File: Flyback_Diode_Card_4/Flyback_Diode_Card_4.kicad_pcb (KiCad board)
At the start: 2 copper layers, 68 parts, among them J1 Screw_Terminal_01x06, J2 Screw_Terminal_01x06, J3 Screw_Terminal_01x02, J4 Screw_Terminal_01x12, J5 Screw_Terminal_01x12, J6 Screw_Terminal_01x04, J7 Screw_Terminal_01x02, J8 Screw_Terminal_01x02

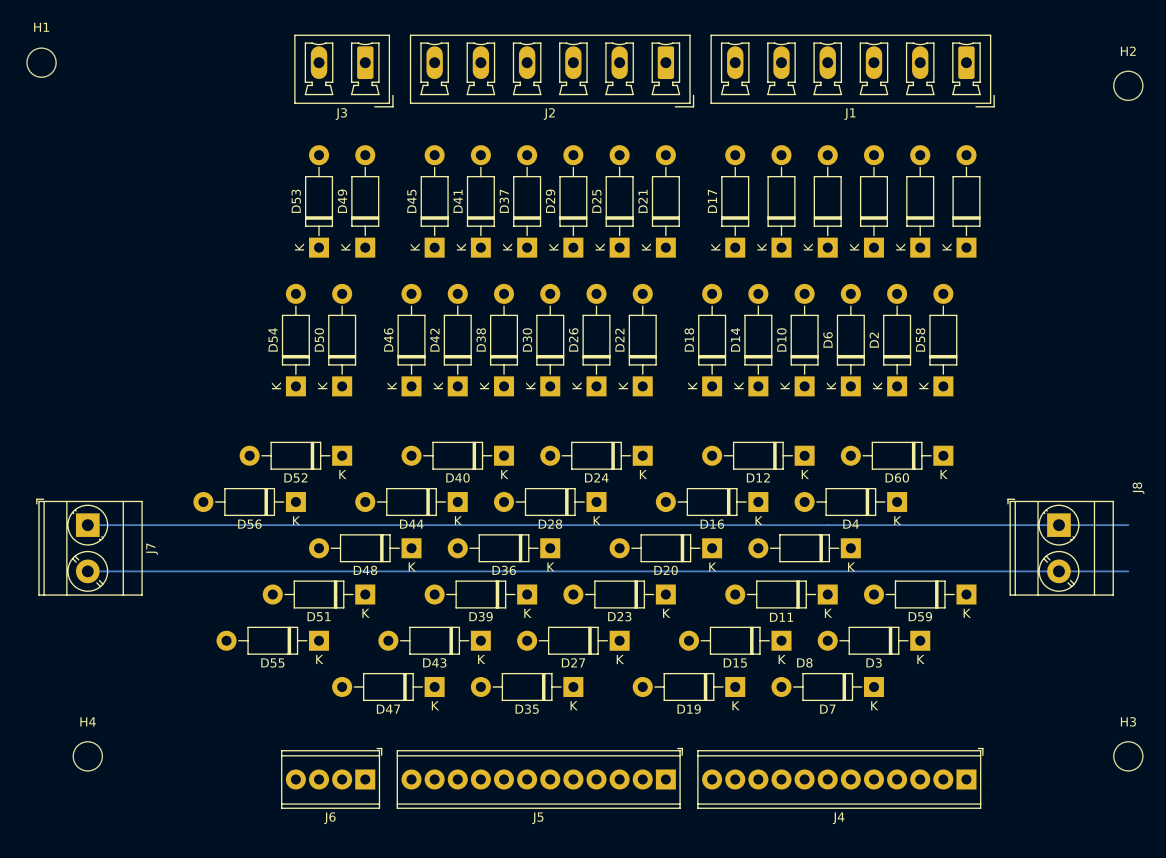
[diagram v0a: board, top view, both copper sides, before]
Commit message: Working on new flyback diode card/
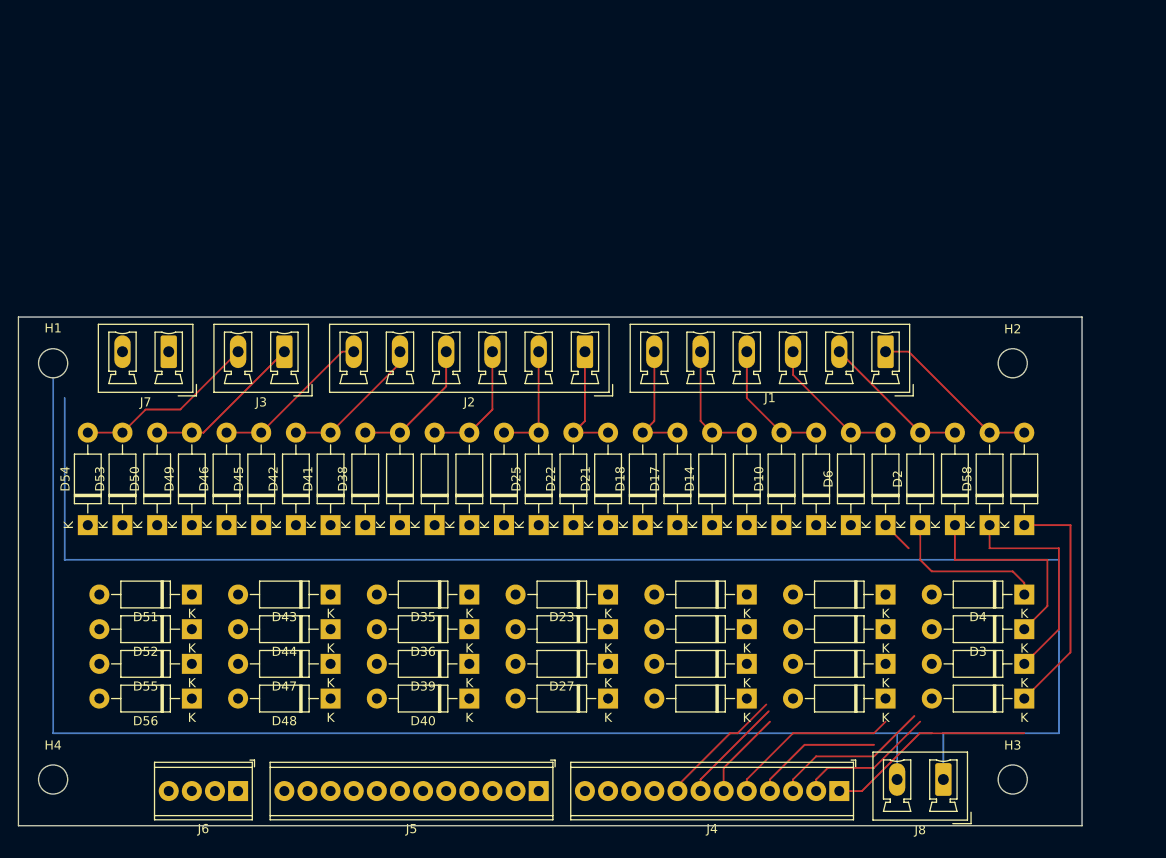
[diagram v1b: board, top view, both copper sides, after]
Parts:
- J7, J8: footprint TerminalBlock_Phoenix:TerminalBlock_Phoenix_MKDS-3-2-5.08_1x02_P5.08mm_Horizontal -> Connector_Phoenix_MC_HighVoltage:PhoenixContact_MCV_1,5_2-G-5.08_1x02_P5.08mm_Vertical
- moved D53 37.4 mm to (87.6, 94.0)
- moved D45 35.9 mm to (102.9, 94.0)
- moved D49 35.9 mm to (95.2, 94.0)
- moved D41 34.7 mm to (110.5, 94.0)
- moved D37 33.5 mm to (118.1, 94.0)
- moved H1 33.0 mm to (80.0, 76.2)
- moved H2 33.0 mm to (185.4, 76.2)
- moved J1 33.0 mm to (171.4, 74.9)
- moved J3 33.0 mm to (105.4, 74.9)
- moved J2 33.0 mm to (138.4, 74.9)
- moved D29 32.6 mm to (125.7, 94.0)
- moved D25 31.8 mm to (133.3, 94.0)
- moved D17 31.1 mm to (148.6, 94.0)
- moved D21 31.1 mm to (141.0, 94.0)
- moved D57 31.1 mm to (186.7, 94.0)
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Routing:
- net /Tens_Common: track 114.3 -> 163.8 mm
- net /A1_Set: track 0.00 -> 49.2 mm
- net /A1_Reset: track 0.00 -> 40.1 mm
- net /A10_Set: track 0.00 -> 39.8 mm
- net /A10_Reset: track 0.00 -> 31.8 mm
- net /Unit_Common: track 114.3 -> 143.5 mm
- net /B1_Set: track 0.00 -> 22.7 mm
- net /G_Reset: track 0.00 -> 20.2 mm
- net /A_Set: track 0.00 -> 18.9 mm
- net /G_Set: track 0.00 -> 17.7 mm
- net /F_Reset: track 0.00 -> 17.7 mm
- net /A_Reset: track 0.00 -> 16.4 mm
- net /F_Set: track 0.00 -> 15.9 mm
- net /B_Set: track 0.00 -> 15.3 mm
- net /E_Reset: track 0.00 -> 14.8 mm
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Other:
- board outline added: 116.8 x 55.9 mm

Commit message: Finished and submitted for manufacturing  New PCB Flyback Board
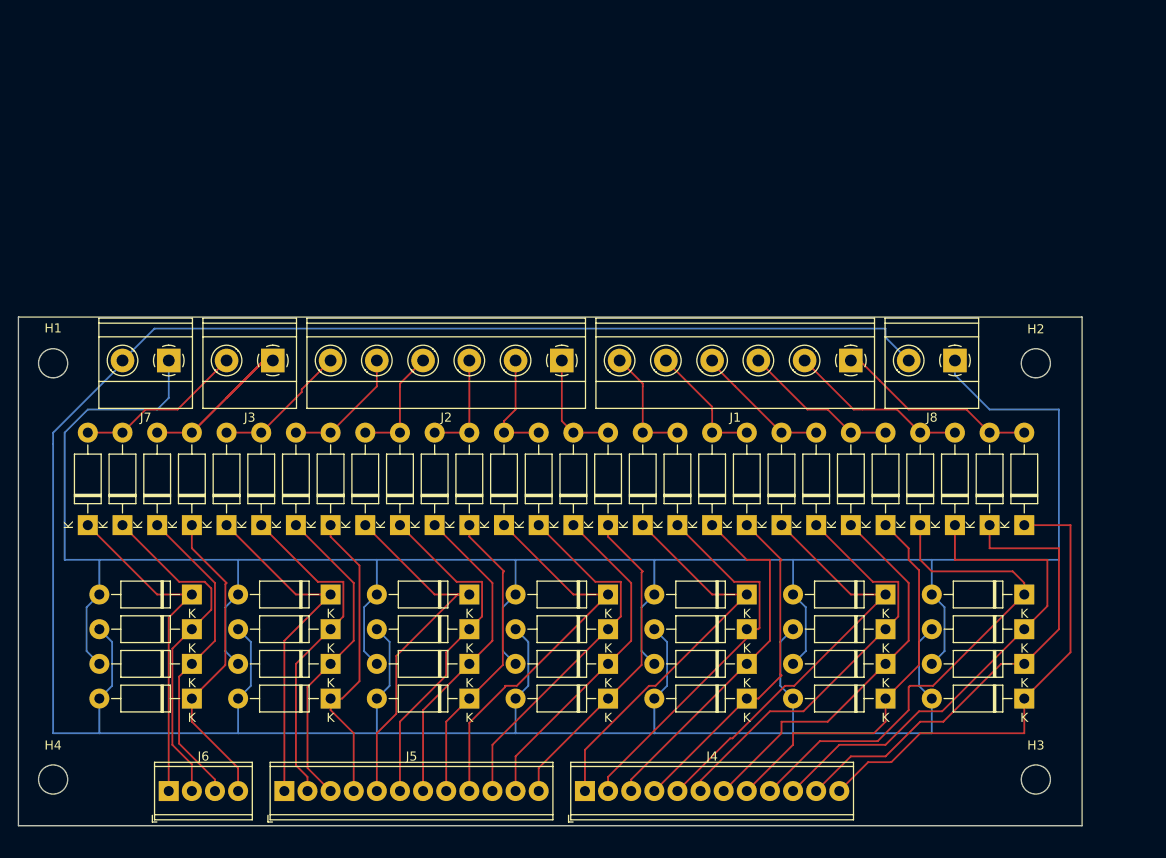
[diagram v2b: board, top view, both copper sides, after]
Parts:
- J1, J2: footprint Connector_Phoenix_MC_HighVoltage:PhoenixContact_MCV_1,5_6-G-5.08_1x06_P5.08mm_Vertical -> TerminalBlock_Phoenix:TerminalBlock_Phoenix_MKDS-1,5-6-5.08_1x06_P5.08mm_Horizontal
- J3, J7, J8: footprint Connector_Phoenix_MC_HighVoltage:PhoenixContact_MCV_1,5_2-G-5.08_1x02_P5.08mm_Vertical -> TerminalBlock_Phoenix:TerminalBlock_Phoenix_MKDS-1,5-2-5.08_1x02_P5.08mm_Horizontal
- moved J8 46.0 mm to (179.1, 75.9)
- moved J4 27.9 mm to (138.4, 123.2), turned to 0 degrees
- moved J5 27.9 mm to (105.4, 123.2), turned to 0 degrees
- moved D23 11.4 mm to (141.0, 113.0)
- moved D28 11.4 mm to (141.0, 101.6)
- moved D35 11.4 mm to (125.7, 113.0)
- moved D40 11.4 mm to (125.7, 101.6)
- moved D43 11.4 mm to (110.5, 113.0)
- moved D48 11.4 mm to (110.5, 101.6)
- moved D51 11.4 mm to (95.2, 113.0)
- moved D56 11.4 mm to (95.2, 101.6)
- moved J6 7.62 mm to (92.7, 123.2), turned to 0 degrees
- moved J1 3.93 mm to (167.6, 75.9)
- moved D24 3.81 mm to (141.0, 109.2)
- moved D27 3.81 mm to (141.0, 105.4)
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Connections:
- J4 pad 1: /A1_Set -> /C10_Reset
- J4 pad 10: /C10_Set -> /A1_Reset
- J4 pad 11: /C1_Reset -> /A10_Set
- J4 pad 12: /C10_Reset -> /A1_Set
- J4 pad 2: /A10_Set -> /C1_Reset
- J4 pad 3: /A1_Reset -> /C10_Set
- J4 pad 4: /A10_Reset -> /C1_Set
- J4 pad 5: /B1_Set -> /B10_Reset
- J4 pad 6: /B10_Set -> /B1_Reset
- J4 pad 7: /B1_Reset -> /B10_Set
- J4 pad 8: /B10_Reset -> /B1_Set
- J4 pad 9: /C1_Set -> /A10_Reset
- J5 pad 1: /D1_Set -> /F10_Reset
- J5 pad 10: /F10_Set -> /D1_Reset
- J5 pad 11: /F1_Reset -> /D10_Set
- J5 pad 12: /F10_Reset -> /D1_Set
- J5 pad 2: /D10_Set -> /F1_Reset
- J5 pad 3: /D1_Reset -> /F10_Set
- J5 pad 4: /D10_Reset -> /F1_Set
- J5 pad 5: /E1_Set -> /E10_Reset
- J5 pad 6: /E10_Set -> /E1_Reset
- J5 pad 7: /E1_Reset -> /E10_Set
- J5 pad 8: /E10_Reset -> /E1_Set
- J5 pad 9: /F1_Set -> /D10_Reset
- J6 pad 1: /G1_Set -> /G10_Reset
- J6 pad 2: /G10_Set -> /G1_Reset
- J6 pad 3: /G1_Reset -> /G10_Set
- J6 pad 4: /G10_Reset -> /G1_Set
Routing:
- net /Unit_Common: track 143.5 -> 319.5 mm
- net /Tens_Common: track 163.8 -> 260.5 mm
- net /C10_Reset: track 0.00 -> 44.0 mm
- net /D10_Reset: track 0.00 -> 43.2 mm
- net /C1_Reset: track 0.00 -> 42.2 mm
- net /E10_Reset: track 0.00 -> 41.1 mm
- net /D1_Reset: track 0.00 -> 40.4 mm
- net /C10_Set: track 0.00 -> 39.6 mm
- net /E1_Reset: track 0.00 -> 38.3 mm
- net /F10_Reset: track 0.00 -> 38.3 mm
- net /G1_Reset: track 0.00 -> 37.6 mm
- net /C1_Set: track 0.00 -> 37.4 mm
- net /F1_Reset: track 0.00 -> 37.3 mm
- net /G10_Reset: track 0.00 -> 37.2 mm
- net /D10_Set: track 0.00 -> 37.1 mm
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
